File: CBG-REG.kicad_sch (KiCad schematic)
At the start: 36 parts, among them J1 Conn_01x09_Socket, J2 Conn_01x09_Socket, U1 AD8560ACP-REEL7, U2 AD8560ACP-REEL7, U4 74LVC2G04

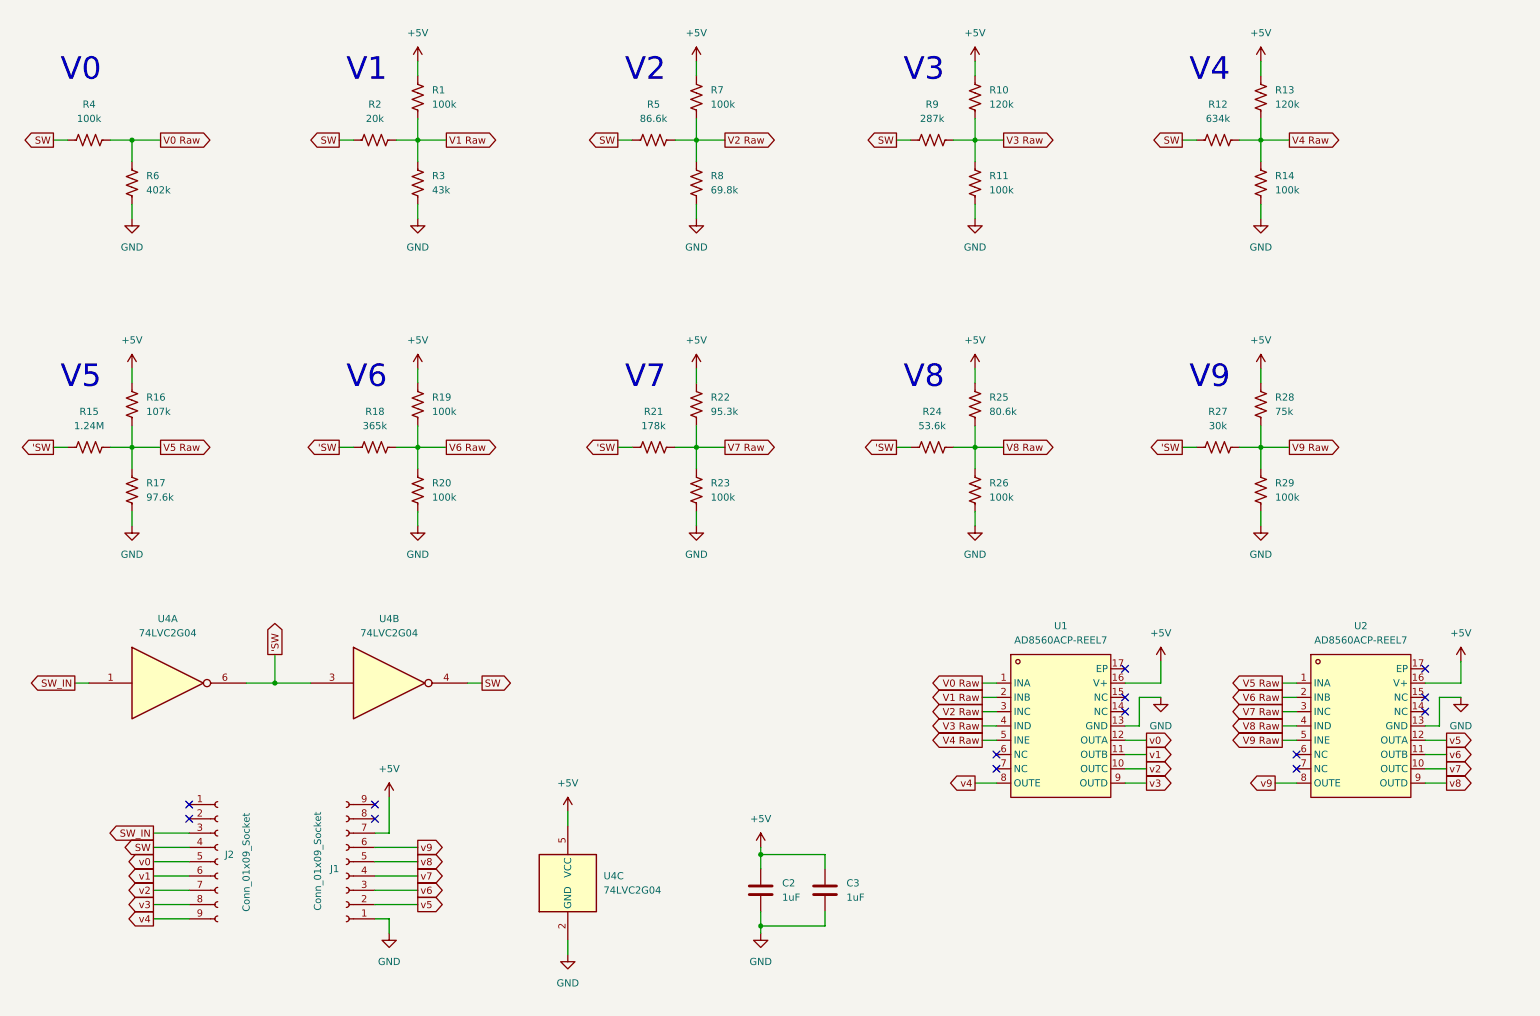
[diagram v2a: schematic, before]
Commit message: feat: Redesign the board to use an IC that JLCPCB has in stock
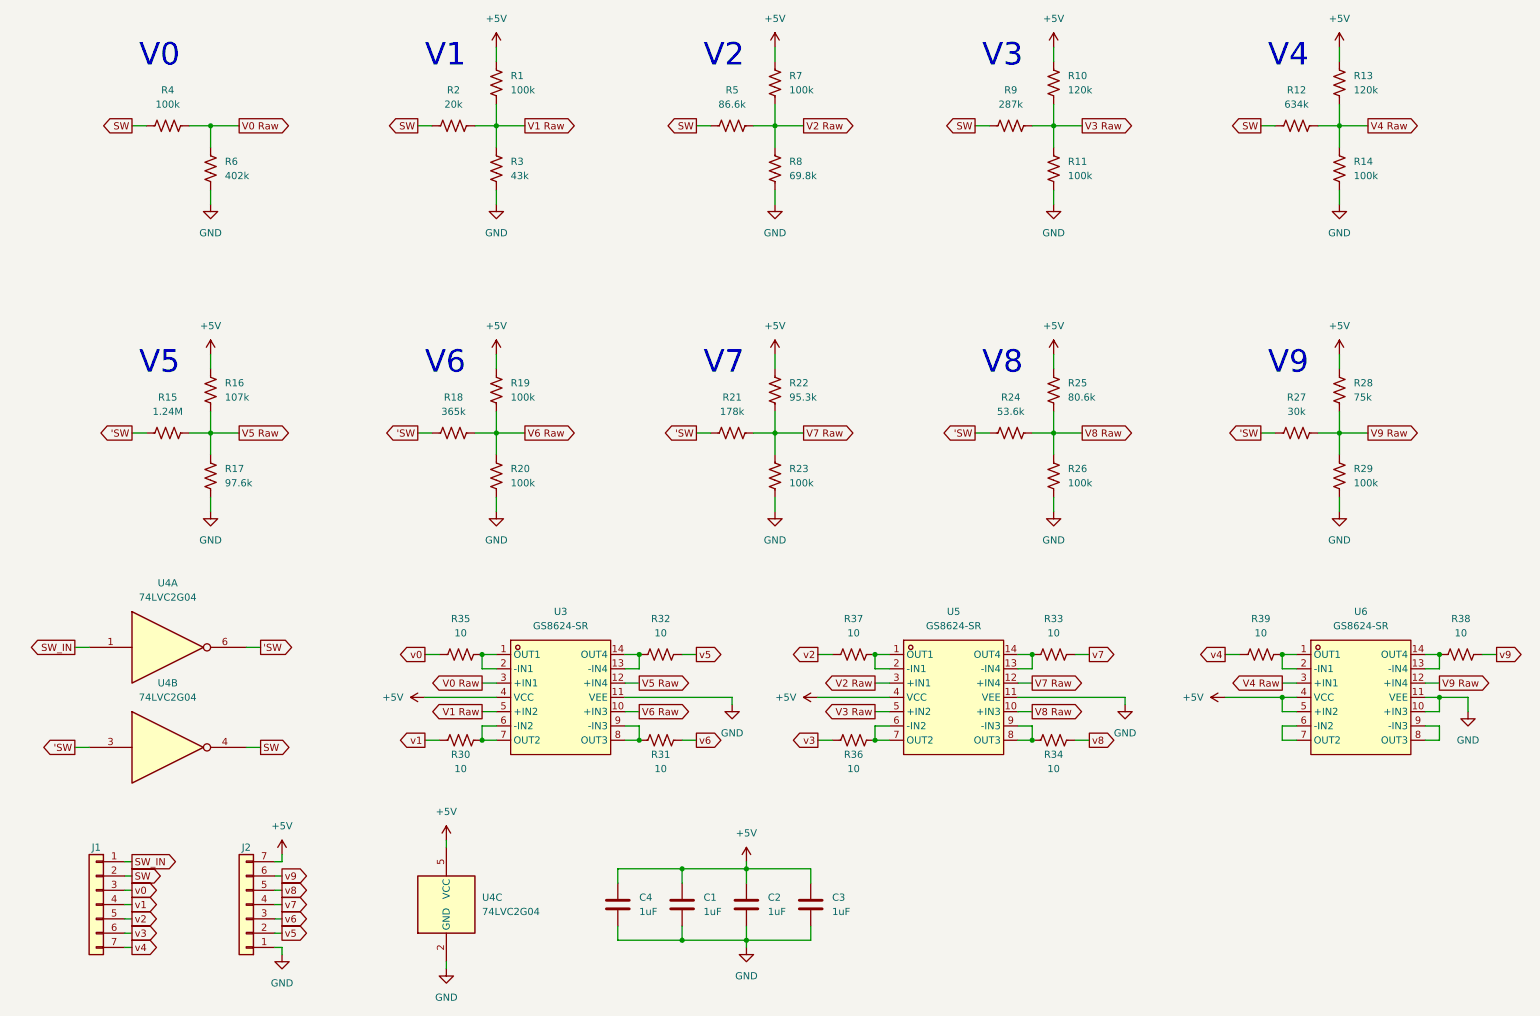
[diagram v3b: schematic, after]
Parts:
- removed J1, J2: Conn_01x09_Socket, Connector_PinHeader_2.00mm:PinHeader_1x09_P2.00mm_Vertical, symbol Connector:Conn_01x09_Socket
- removed U1, U2: AD8560ACP-REEL7, easyeda2kicad:LFCSP-16_L4.0-W4.0-P0.65-TL-EP2.2, symbol easyeda2kicad:AD8560ACP-REEL7
- added C1, C4: 1uF, Capacitor_SMD:C_0603_1608Metric, symbol Device:C
- added J1, J2: Conn_01x07, Connector_PinHeader_2.54mm:PinHeader_1x07_P2.54mm_Vertical, symbol Connector_Generic:Conn_01x07
- added R30, R31, R32, R33, R34, R35, R36, R37, R38, R39: 10, Resistor_SMD:R_0603_1608Metric, symbol Device:R_US
- added U3, U5, U6: GS8624-SR, easyeda2kicad:SOIC-14_L8.6-W3.9-P1.27-LS6.0-BL, symbol easyeda2kicad:GS8624-SR
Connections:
- net +5V: now also C1.1, C4.1, J2.7 (Pin_7), U3.4 (VCC), U5.4 (VCC), U6.4 (VCC), U6.5 (+IN2)
- net GND: now also C1.2, C4.2, J2.1 (Pin_1), U3.11 (VEE), U5.11 (VEE), U6.10 (+IN3), U6.11 (VEE)
- net SW: now also J1.2 (Pin_2)
- net SW_IN: now also J1.1 (Pin_1)
- net V0 Raw: now also U3.3 (+IN1)
- net V1 Raw: now also U3.5 (+IN2)
- net V2 Raw: now also U5.3 (+IN1)
- net V3 Raw: now also U5.5 (+IN2)
- net V4 Raw: now also U6.3 (+IN1)
- net V5 Raw: now also U3.12 (+IN4)
- net V6 Raw: now also U3.10 (+IN3)
- net V7 Raw: now also U5.12 (+IN4)
- net V8 Raw: now also U5.10 (+IN3)
- net V9 Raw: now also U6.12 (+IN4)
- net v0: now also J1.3 (Pin_3), R35.1
- net v1: now also J1.4 (Pin_4), R30.1
- net v2: now also J1.5 (Pin_5), R37.1
- net v3: now also J1.6 (Pin_6), R36.1
- net v4: now also J1.7 (Pin_7), R39.1
- net v5: now also J2.2 (Pin_2), R32.2
- net v6: now also J2.3 (Pin_3), R31.2
- net v7: now also J2.4 (Pin_4), R33.2
- net v8: now also J2.5 (Pin_5), R34.2
- net v9: now also J2.6 (Pin_6), R38.1
- new net: R37.2, U5.1 (OUT1), U5.2 (-IN1)
- new net: R39.2, U6.1 (OUT1), U6.2 (-IN1)
- new net: R35.2, U3.1 (OUT1), U3.2 (-IN1)
- new net: R38.2, U6.13 (-IN4), U6.14 (OUT4)
- new net: R33.1, U5.13 (-IN4), U5.14 (OUT4)
- new net: R32.1, U3.13 (-IN4), U3.14 (OUT4)
- new net: R30.2, U3.6 (-IN2), U3.7 (OUT2)
- new net: R31.1, U3.8 (OUT3), U3.9 (-IN3)
- new net: U6.6 (-IN2), U6.7 (OUT2)
- new net: U6.8 (OUT3), U6.9 (-IN3)
- new net: R36.2, U5.6 (-IN2), U5.7 (OUT2)
- new net: R34.1, U5.8 (OUT3), U5.9 (-IN3)
- no-connect marks 14 -> 0
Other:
- moved on the sheet: C2, C3, R1, R10, R11, R12, R13, R14, R15, R16, R17, R18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
